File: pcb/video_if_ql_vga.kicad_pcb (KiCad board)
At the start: 2 copper layers, 31.1 x 66.2 mm, 16 parts, among them J1 Conn_01x05, J2 DB15_Female_HighDensity, U1 SC0915

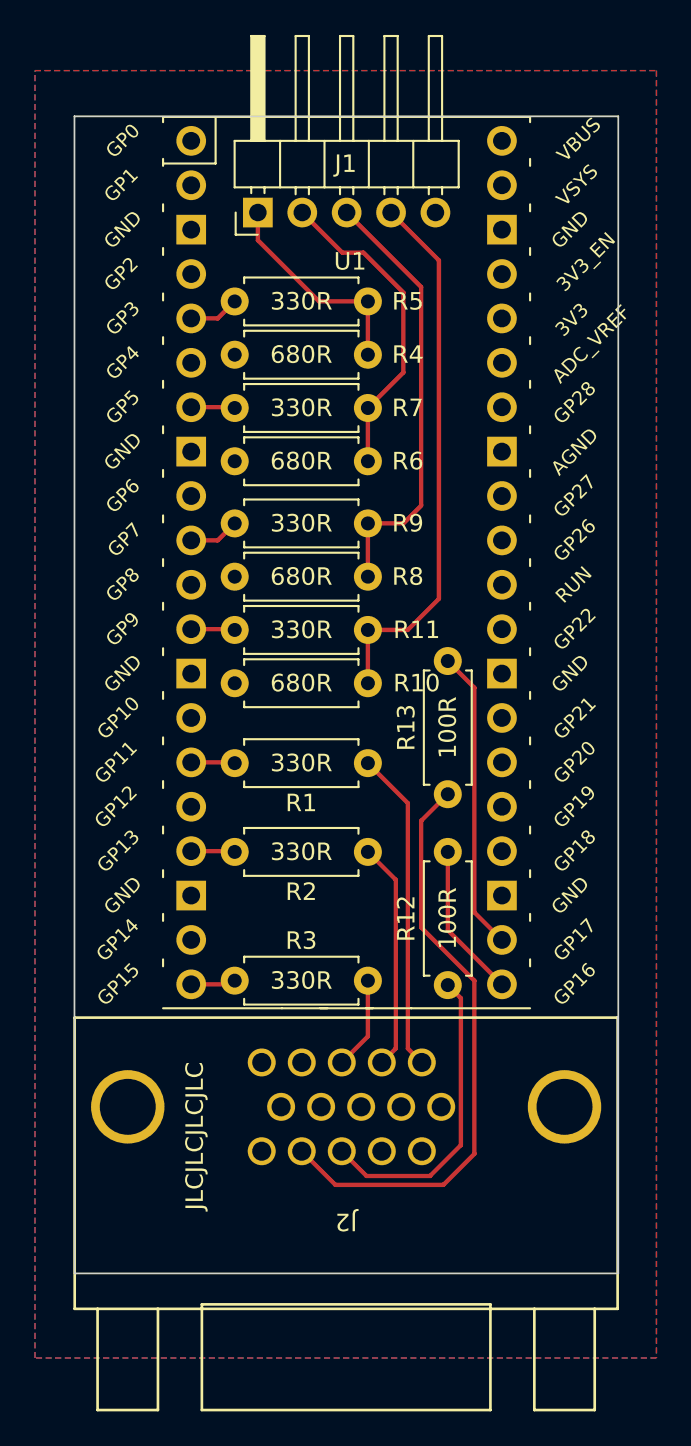
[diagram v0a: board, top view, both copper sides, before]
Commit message: Version 1.0 PCB assembled and tested
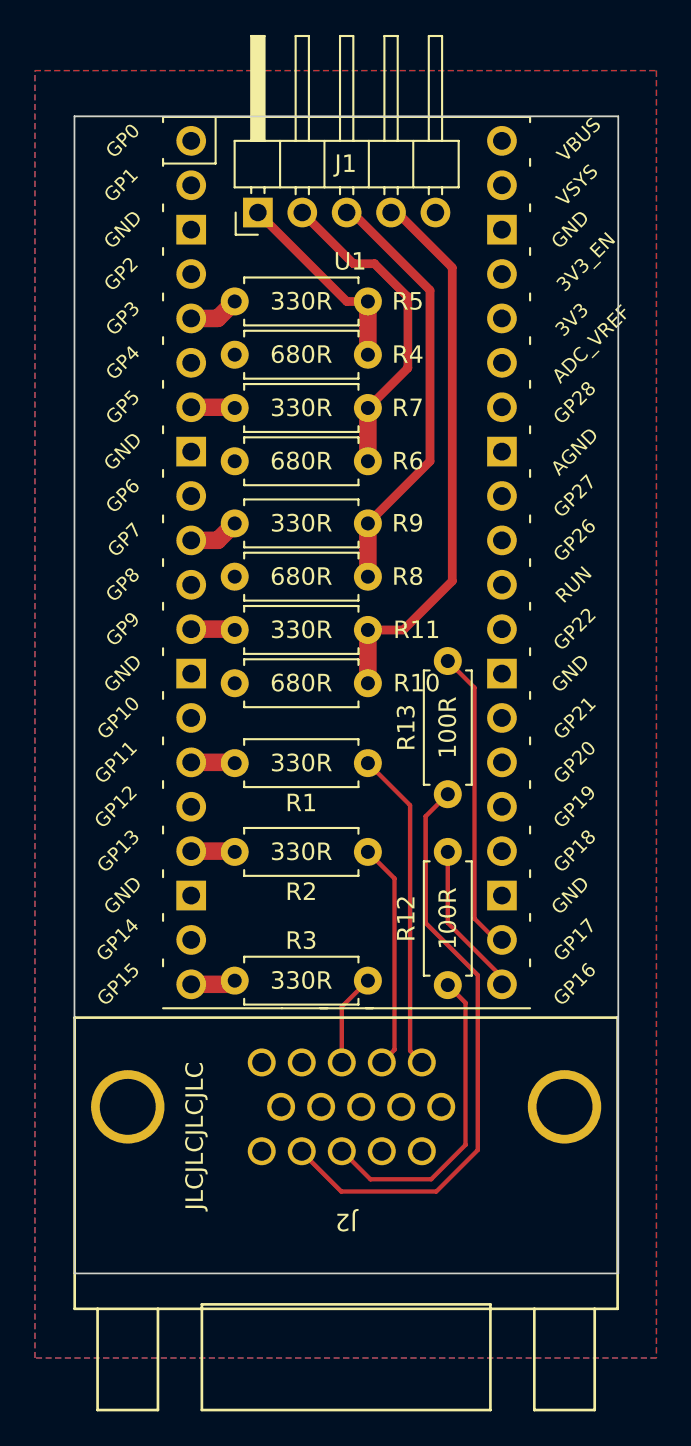
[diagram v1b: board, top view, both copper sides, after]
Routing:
- net Net-(J1-Pad1): track 12.4 -> 11.5 mm
- net Net-(J1-Pad4): track 31.1 -> 31.8 mm
- net Net-(J1-Pad3): track 25.1 -> 24.5 mm
- net Net-(J2-Pad13): track 17.6 -> 18.1 mm
